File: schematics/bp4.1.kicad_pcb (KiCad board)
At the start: 2 copper layers, 90 x 32.6 mm, 39 parts, among them J1 Left Pin Strip, J2 Right Pin Strip, J3 I/O Pin Strip, J4 Power Pins A, J5 Power Pins B, J6 Power Pins C, SW1 Power Switch, U1 TPS61220DCK, U2 LM321

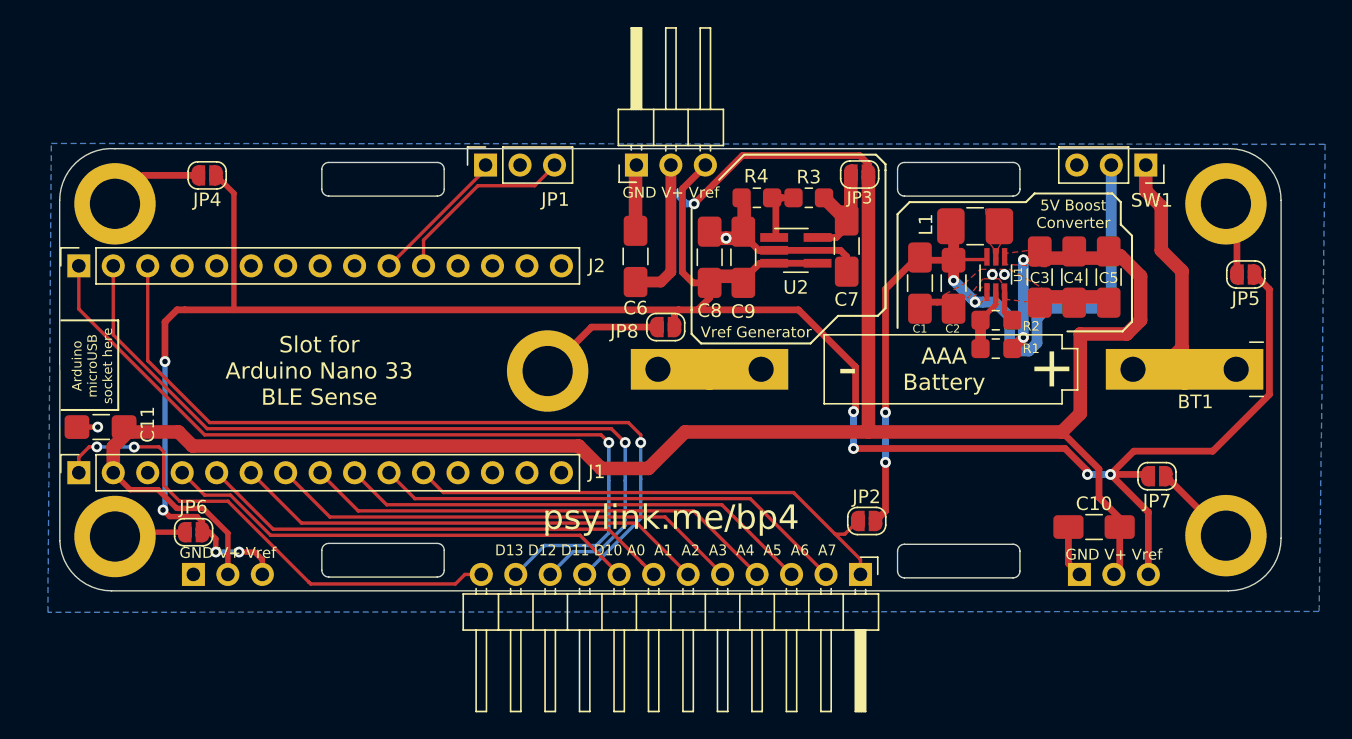
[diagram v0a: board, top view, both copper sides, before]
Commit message: restore original bp4 and rename the updated one to bp4.1
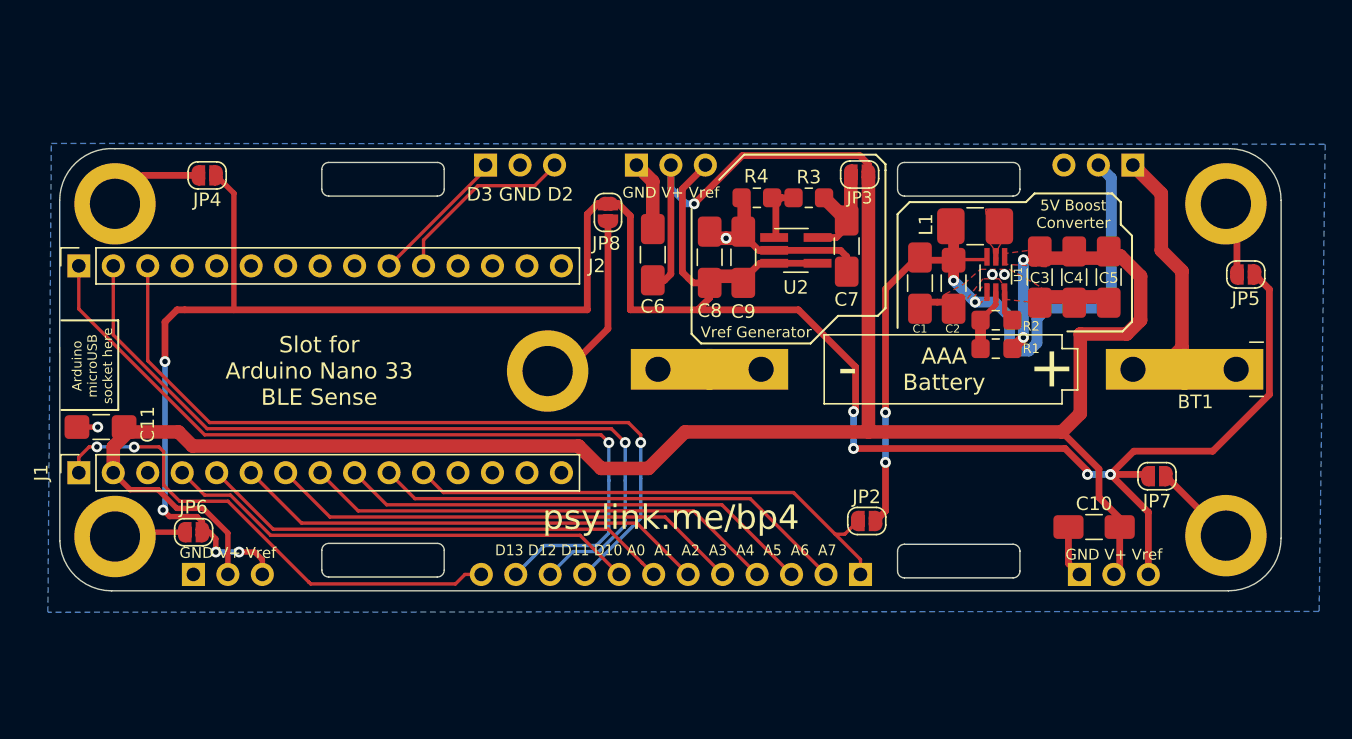
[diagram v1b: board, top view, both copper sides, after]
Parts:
- J3: footprint Connector_PinHeader_2.54mm:PinHeader_1x12_P2.54mm_Horizontal -> Connector_PinHeader_2.54mm:PinHeader_1x12_P2.54mm_Vertical; moved to B.Cu
- J4, J5: footprint Connector_PinHeader_2.54mm:PinHeader_1x03_P2.54mm_Horizontal -> Connector_PinHeader_2.54mm:PinHeader_1x03_P2.54mm_Vertical
- J6: footprint Connector_PinHeader_2.54mm:PinHeader_1x03_P2.54mm_Horizontal -> Connector_PinHeader_2.54mm:PinHeader_1x03_P2.54mm_Vertical; moved to B.Cu
- JP1, SW1: moved to B.Cu
- moved JP8 9.46 mm to (65.8, 30.1), turned to 270 degrees
- moved C6 1.28 mm to (69.1, 33.2)
- moved SW1 0.95 mm to (104.5, 26.6), turned to 90 degrees
- turned J3 to 90 degrees
- turned J6 to 270 degrees
- turned JP1 to 270 degrees
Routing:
- net /Vref: track 171.5 -> 184.8 mm
- net Net-(JP8-Pad2): track 9.39 -> 13.7 mm
- net /V+: track 180.1 -> 178.9 mm
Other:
- board text added: "D3 GND D2"

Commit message: update model name to bp4.1 on silk screen
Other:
- board text added: "psylink.me/bp4.1"
- board text removed: "psylink.me/bp4"
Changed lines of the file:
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@@
   (gr_line (start 25.4 57.9755) (end 115.3795 57.9755) (layer Dwgs.User) (width 0.15))
   (gr_line (start 25.4 25.4) (end 115.3795 25.4) (layer Dwgs.User) (width 0.15))
-  (gr_text psylink.me/bp4 (at 70.4215 52.578) (layer F.SilkS)
+  (gr_text psylink.me/bp4.1 (at 70.4215 52.578) (layer F.SilkS)
     (effects (font (size 1.8 1.8) (thickness 0.35)))
   )
